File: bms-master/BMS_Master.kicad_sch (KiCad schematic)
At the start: 79 parts, among them J1 Conn_PWR, J2 PROG, J4 BMS_M_IN, J5 Conn_CAN, J6 Conn_CSR, J7 Conn_CSROUT, Q1 BC807, SW1 SW_SPST, U1 AP2204K-ADJ, U2 AP2204K-ADJ, U3 STM32F103C8Tx, U4 BQ79600-Q1, U5 SN65HVD256D, U6 TLV2371DBV, U7 TLV2371DBV, Y1 8M, Y2 32.768k

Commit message: Finish bms_master pcb layout
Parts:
- C30, C31: footprint (none) -> Capacitor_SMD:C_0603_1608Metric
- J7: footprint (none) -> Connector_JST:JST_XH_B3B-XH-A_1x03_P2.50mm_Vertical
- R27, R28: footprint (none) -> Resistor_SMD:R_0603_1608Metric
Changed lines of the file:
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@@
       (effects (font (size 1.27 1.27)) (justify left))
     )
-    (property "Footprint" "" (at 147.955 135.255 0)
+    (property "Footprint" "Capacitor_SMD:C_0603_1608Metric" (at 147.955 135.255 0)
       (effects (font (size 1.27 1.27)) hide)
     )
@@
       (effects (font (size 1.27 1.27)) (justify right))
     )
-    (property "Footprint" "" (at 135.255 173.355 0)
+    (property "Footprint" "Resistor_SMD:R_0603_1608Metric" (at 135.255 173.355 0)
       (effects (font (size 1.27 1.27)) hide)
     )
@@
       (effects (font (size 1.27 1.27)) (justify left))
     )
-    (property "Footprint" "" (at 153.035 184.15 0)
+    (property "Footprint" "Connector_JST:JST_XH_B3B-XH-A_1x03_P2.50mm_Vertical" (at 153.035 184.15 0)
       (effects (font (size 1.27 1.27)) hide)
     )
@@
       (effects (font (size 1.27 1.27)) (justify right))
     )
-    (property "Footprint" "" (at 135.255 179.705 0)
+    (property "Footprint" "Resistor_SMD:R_0603_1608Metric" (at 135.255 179.705 0)
       (effects (font (size 1.27 1.27)) hide)
     )
@@
       (effects (font (size 1.27 1.27)) (justify left))
     )
-    (property "Footprint" "" (at 147.955 163.195 0)
+    (property "Footprint" "Capacitor_SMD:C_0603_1608Metric" (at 147.955 163.195 0)
       (effects (font (size 1.27 1.27)) hide)
     )

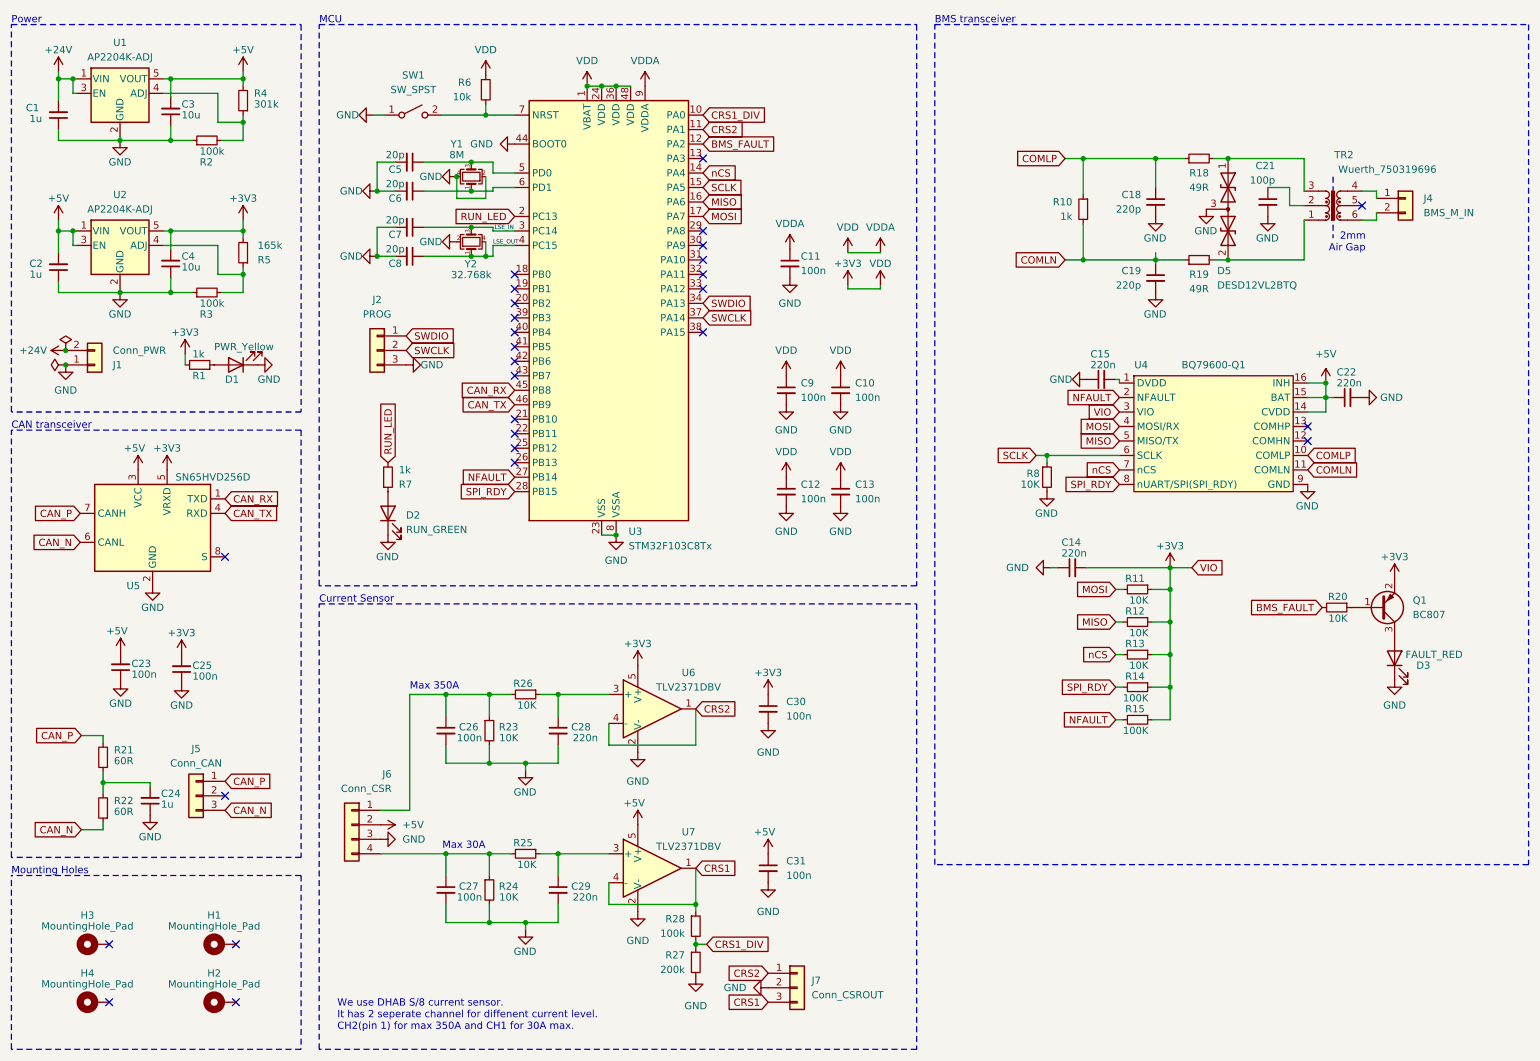
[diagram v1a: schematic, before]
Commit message: Reconfigure file structure and create share lib and 3D CAD
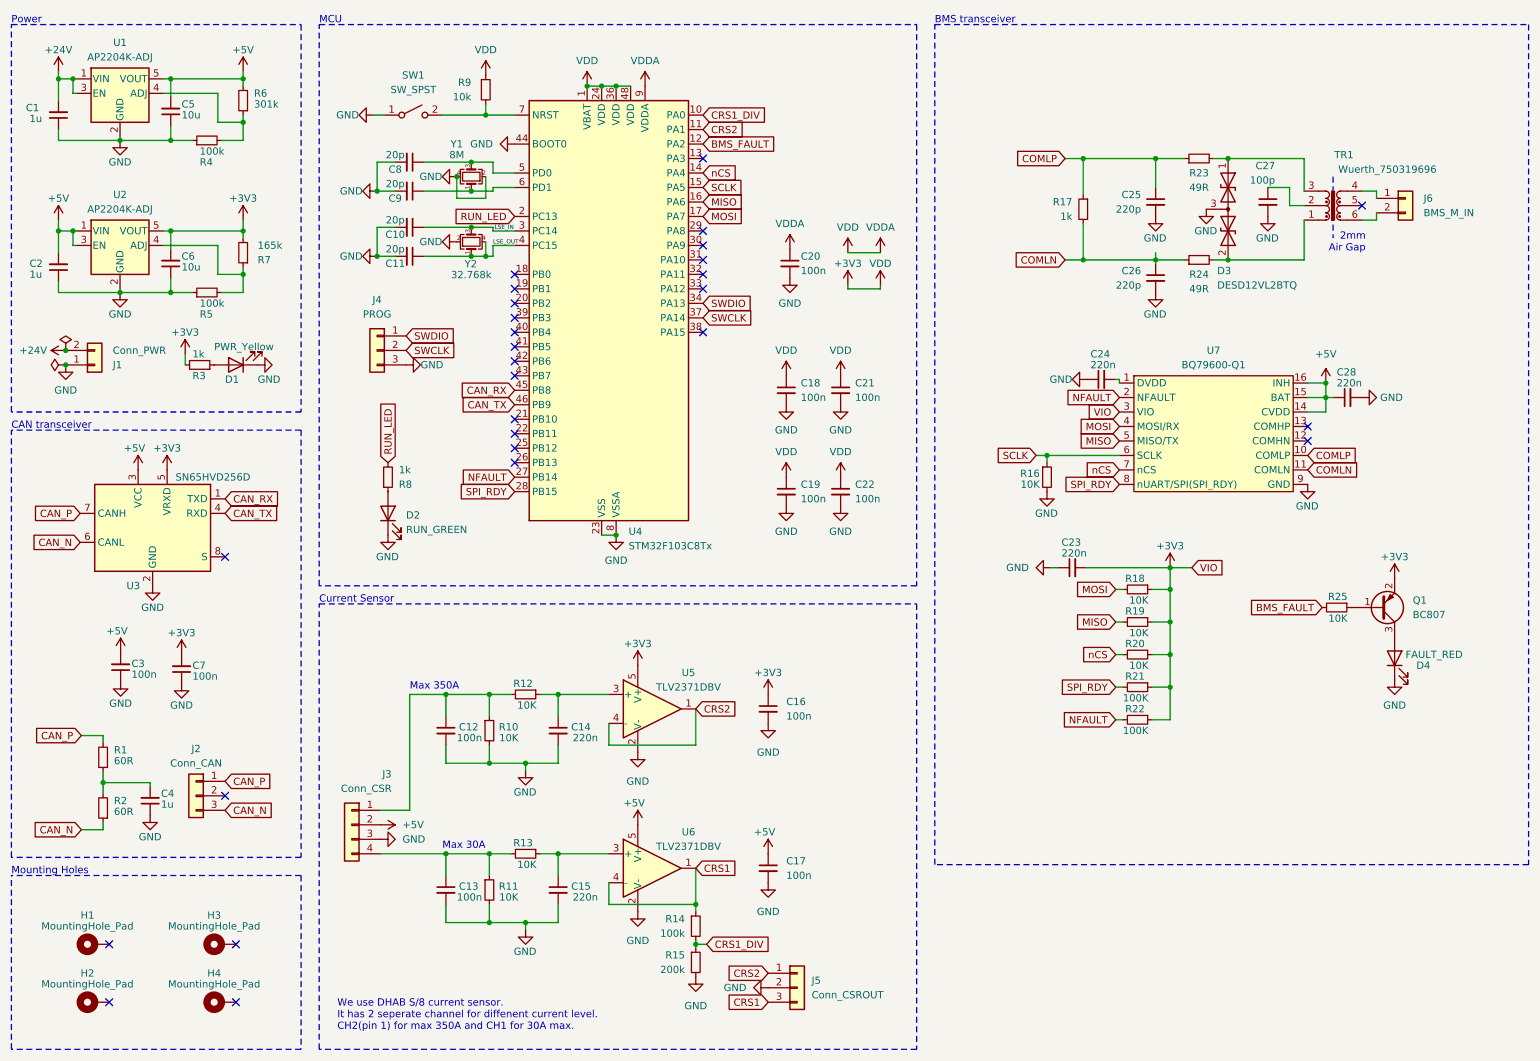
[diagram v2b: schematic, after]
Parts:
- removed U4: BQ79600-Q1, Package_SO:TSSOP-16_4.4x5mm_P0.65mm, symbol Local_Lib:BQ79600-Q1
- added U7: BQ79600-Q1, Package_SO:TSSOP-16_4.4x5mm_P0.65mm, symbol Project_Lib:BQ79600-Q1
- renumbered C7 to C10, C8 to C11, C26 to C12, C27 to C13, C28 to C14, C29 to C15, C30 to C16, C31 to C17, C9 to C18, C12 to C19, C11 to C20, C10 to C21, C13 to C22, C14 to C23, C15 to C24, C18 to C25, C19 to C26, C21 to C27, C22 to C28, C23 to C3, C24 to C4, C3 to C5, C4 to C6, C25 to C7, C5 to C8, C6 to C9, D5 to D3, D3 to D4, H3 to H1, H4 to H2, H1 to H3, H2 to H4, J5 to J2, J6 to J3, J2 to J4, J7 to J5, J4 to J6, R21 to R1, R23 to R10, R24 to R11, R26 to R12, R25 to R13, R28 to R14, R27 to R15, R8 to R16, R10 to R17, R11 to R18, R12 to R19, R22 to R2, R13 to R20, R14 to R21, R15 to R22, R18 to R23, R19 to R24, R20 to R25, R1 to R3, R2 to R4, R3 to R5, R4 to R6, R5 to R7, R7 to R8, R6 to R9, TR2 to TR1, U5 to U3, U3 to U4, U6 to U5, U7 to U6
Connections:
- net +3V3: now also U7.3 (VIO)
- net +5V: now also U7.14 (CVDD), U7.15 (BAT), U7.16 (INH)
- net COMLN: now also U7.11 (COMLN)
- net COMLP: now also U7.10 (COMLP)
- net GND: now also U7.9 (GND)
- net MISO: now also U7.5 (MISO/TX)
- net MOSI: now also U7.4 (MOSI/RX)
- net NFAULT: now also U7.2 (NFAULT)
- net SCLK: now also U7.6 (SCLK)
- net SPI_RDY: now also U7.8 (nUART/SPI(SPI_RDY))
- net nCS: now also U7.7 (nCS)
- net at C24.2: now also U7.1 (DVDD)

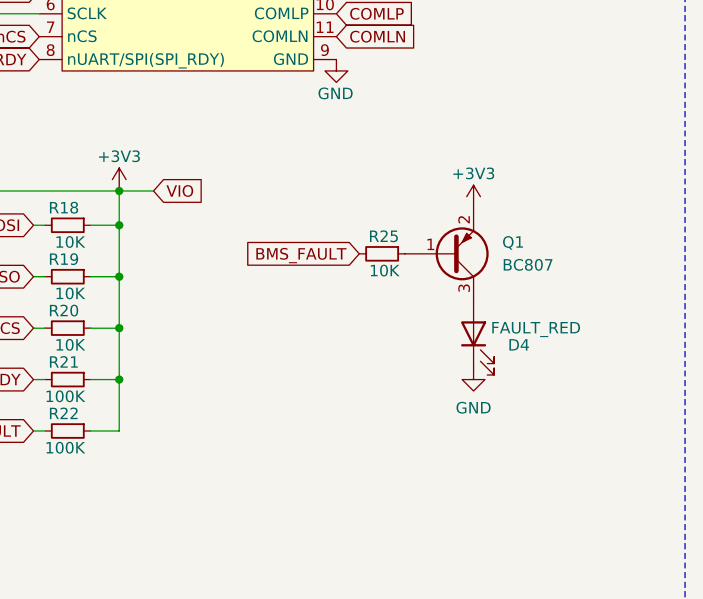
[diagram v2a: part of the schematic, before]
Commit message: fix: add bms fault connector
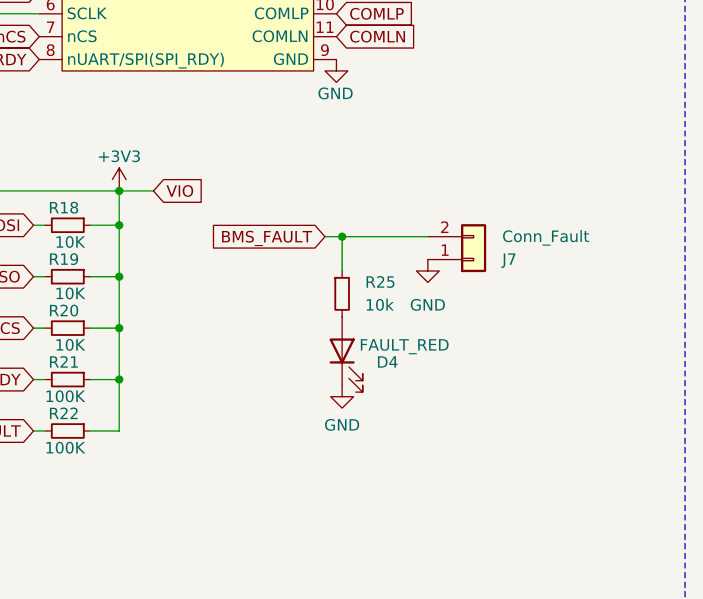
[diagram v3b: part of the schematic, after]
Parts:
- removed Q1: BC807, Package_TO_SOT_SMD:SOT-23, symbol Transistor_BJT:BC807
- added J7: Conn_Fault, Connector_JST:JST_XH_B2B-XH-A_1x02_P2.50mm_Vertical, symbol Connector_Generic:Conn_01x02
- R25: value 10K -> 10k
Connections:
- net BMS_FAULT: now also R25.1, J7.2 (Pin_2); no longer R25.2
- net GND: now also J7.1 (Pin_1)
- net at D4.2 (A): now also R25.2
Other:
- moved on the sheet: D4
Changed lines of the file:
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@@
   (junction (at 93.345 41.91) (diameter 0) (color 0 0 0 0)
   )
+  (junction (at 243.205 115.57) (diameter 0) (color 0 0 0 0)
+  )
   (junction (at 121.285 104.775) (diameter 0) (color 0 0 0 0)
   )
@@
     (stroke (width 0) (type default))
   )
+  (wire (pts (xy 243.205 115.57) (xy 252.73 115.57))
+    (stroke (width 0) (type default))
+  )
   (wire (pts (xy 43.18 51.435) (xy 43.18 54.61))
     (stroke (width 0) (type default))
@@
     (stroke (width 0) (type default))
   )
+  (wire (pts (xy 241.3 115.57) (xy 243.205 115.57))
+    (stroke (width 0) (type default))
+  )
   (wire (pts (xy 239.395 43.815) (xy 235.585 43.815))
     (stroke (width 0) (type default))
@@
     (stroke (width 0) (type default))
   )
+  (wire (pts (xy 243.205 115.57) (xy 243.205 119.38))
+    (stroke (width 0) (type default))
+  )
   (wire (pts (xy 31.3182 155.1686) (xy 31.3182 156.4386))
     (stroke (width 0) (type default))
@@
     (effects (font (size 0.735 0.735)) (justify left bottom))
   )
-  (global_label "BMS_FAULT" (shape input) (at 245.11 117.475 180) (fields_autoplaced)
+  (global_label "BMS_FAULT" (shape input) (at 241.3 115.57 180) (fields_autoplaced)
     (effects (font (size 1.27 1.27)) (justify right))
-    (property "Intersheetrefs" "${INTERSHEET_REFS}" (at 231.7229 117.475 0)
+    (property "Intersheetrefs" "${INTERSHEET_REFS}" (at 227.9129 115.57 0)
       (effects (font (size 1.27 1.27)) (justify right) hide)
     )
@@
     )
   )
-  (symbol (lib_id "power:GND") (at 257.81 130.175 0) (unit 1)
+  (symbol (lib_id "power:GND") (at 243.205 132.08 0) (unit 1)
     (in_bom yes) (on_board yes) (dnp no) (fields_autoplaced)
-    (property "Reference" "#PWR071" (at 257.81 136.525 0)
+    (property "Reference" "#PWR071" (at 243.205 138.43 0)
       (effects (font (size 1.27 1.27)) hide)
     )
-    (property "Value" "GND" (at 257.81 134.62 0)
+    (property "Value" "GND" (at 243.205 136.525 0)
       (effects (font (size 1.27 1.27)))
     )
-    (property "Footprint" "" (at 257.81 130.175 0)
+    (property "Footprint" "" (at 243.205 132.08 0)
       (effects (font (size 1.27 1.27)) hide)
     )
-    (property "Datasheet" "" (at 257.81 130.175 0)
+    (property "Datasheet" "" (at 243.205 132.08 0)
       (effects (font (size 1.27 1.27)) hide)
     )
@@
     )
   )
+  (symbol (lib_id "power:GND") (at 252.73 118.11 0) (unit 1)
+    (in_bom yes) (on_board yes) (dnp no) (fields_autoplaced)
+    (property "Reference" "#PWR070" (at 252.73 124.46 0)
+      (effects (font (size 1.27 1.27)) hide)
+    )
+    (property "Value" "GND" (at 252.73 123.19 0)
+      (effects (font (size 1.27 1.27)))
+    )
+    (property "Footprint" "" (at 252.73 118.11 0)
+      (effects (font (size 1.27 1.27)) hide)
+    )
+    (property "Datasheet" "" (at 252.73 118.11 0)
+      (effects (font (size 1.27 1.27)) hide)
+    )
+    (pin "1")
+    (instances
+      (project "BMS_Master"
+        (path "/a5fe69d4-6cf1-475c-8d8a-0453004bba44"
+          (reference "#PWR070") (unit 1)
+        )
+      )
+    )
+  )
   (symbol (lib_id "power:+5V") (at 55.88 23.495 0) (unit 1)
     (in_bom yes) (on_board yes) (dnp no)
@@
     )
   )
-  (symbol (lib_id "Device:C_Small") (at 45.085 128.27 180) (unit 1)
-    (in_bom yes) (on_board yes) (dnp no)
-    (property "Reference" "C7" (at 46.99 127.635 0)
-      (effects (font (size 1.27 1.27)) (justify right))
+  (symbol (lib_id "Device:R_Small") (at 243.205 121.92 0) (unit 1)
+    (in_bom yes) (on_board yes) (dnp no) (fields_autoplaced)
+    (property "Reference" "R25" (at 245.745 120.65 0)
+      (effects (font (size 1.27 1.27)) (justify left))
     )
-    (property "Value" "100n" (at 46.99 129.54 0)
-      (effects (font (size 1.27 1.27)) (justify right))
+    (property "Value" "10k" (at 245.745 123.19 0)
+      (effects (font (size 1.27 1.27)) (justify left))
     )
-    (property "Footprint" "Capacitor_SMD:C_0603_1608Metric" (at 45.085 128.27 0)
+    (property "Footprint" "Resistor_SMD:R_0603_1608Metric" (at 243.205 121.92 0)
       (effects (font (size 1.27 1.27)) hide)
     )
-    (property "Datasheet" "~" (at 45.085 128.27 0)
+    (property "Datasheet" "~" (at 243.205 121.92 0)
       (effects (font (size 1.27 1.27)) hide)
     )
-    (pin "2")
     (pin "1")
+    (pin "2")
     (instances
       (project "BMS_Master"
         (path "/a5fe69d4-6cf1-475c-8d8a-0453004bba44"
-          (reference "C7") (unit 1)
+          (reference "R25") (unit 1)
         )
       )
     )
   )
-  (symbol (lib_id "Device:R_Small") (at 247.65 117.475 270) (unit 1)
+  (symbol (lib_id "Device:C_Small") (at 45.085 128.27 180) (unit 1)
     (in_bom yes) (on_board yes) (dnp no)
-    (property "Reference" "R25" (at 249.555 115.57 90)
+    (property "Reference" "C7" (at 46.99 127.635 0)
       (effects (font (size 1.27 1.27)) (justify right))
     )
-    (property "Value" "10K" (at 249.555 119.38 90)
+    (property "Value" "100n" (at 46.99 129.54 0)
       (effects (font (size 1.27 1.27)) (justify right))
     )
-    (property "Footprint" "Resistor_SMD:R_0603_1608Metric" (at 247.65 117.475 0)
+    (property "Footprint" "Capacitor_SMD:C_0603_1608Metric" (at 45.085 128.27 0)
       (effects (font (size 1.27 1.27)) hide)
     )
-    (property "Datasheet" "~" (at 247.65 117.475 0)
+    (property "Datasheet" "~" (at 45.085 128.27 0)
       (effects (font (size 1.27 1.27)) hide)
     )
@@
       (project "BMS_Master"
         (path "/a5fe69d4-6cf1-475c-8d8a-0453004bba44"
-          (reference "R25") (unit 1)
+          (reference "C7") (unit 1)
         )
       )
@@
     )
   )
-  (symbol (lib_id "power:+3V3") (at 257.81 112.395 0) (unit 1)
-    (in_bom yes) (on_board yes) (dnp no)
-    (property "Reference" "#PWR070" (at 257.81 116.205 0)
-      (effects (font (size 1.27 1.27)) hide)
-    )
-    (property "Value" "+3V3" (at 257.81 108.585 0)
-      (effects (font (size 1.27 1.27)))
-    )
-    (property "Footprint" "" (at 257.81 112.395 0)
-      (effects (font (size 1.27 1.27)) hide)
-    )
-    (property "Datasheet" "" (at 257.81 112.395 0)
-      (effects (font (size 1.27 1.27)) hide)
-    )
-    (pin "1")
-    (instances
-      (project "BMS_Master"
-        (path "/a5fe69d4-6cf1-475c-8d8a-0453004bba44"
-          (reference "#PWR070") (unit 1)
-        )
-      )
-    )
-  )
   (symbol (lib_id "power:GND") (at 197.485 110.49 270) (unit 1)
     (in_bom yes) (on_board yes) (dnp no)
@@
     )
   )
-  (symbol (lib_id "Device:LED") (at 257.81 126.365 90) (unit 1)
+  (symbol (lib_id "Device:LED") (at 243.205 128.27 90) (unit 1)
     (in_bom yes) (on_board yes) (dnp no)
-    (property "Reference" "D4" (at 261.62 127.635 90)
+    (property "Reference" "D4" (at 247.015 129.54 90)
       (effects (font (size 1.27 1.27)) (justify right))
     )
-    (property "Value" "FAULT_RED" (at 259.715 125.73 90)
+    (property "Value" "FAULT_RED" (at 245.11 127.635 90)
       (effects (font (size 1.27 1.27)) (justify right))
     )
-    (property "Footprint" "LED_SMD:LED_0805_2012Metric" (at 257.81 126.365 0)
+    (property "Footprint" "LED_SMD:LED_0805_2012Metric" (at 243.205 128.27 0)
       (effects (font (size 1.27 1.27)) hide)
     )
-    (property "Datasheet" "~" (at 257.81 126.365 0)
+    (property "Datasheet" "~" (at 243.205 128.27 0)
       (effects (font (size 1.27 1.27)) hide)
     )
@@
     )
   )
+  (symbol (lib_id "Connector_Generic:Conn_01x02") (at 257.81 118.11 0) (mirror x) (unit 1)
+    (in_bom yes) (on_board yes) (dnp no)
+    (property "Reference" "J7" (at 260.985 118.11 0)
+      (effects (font (size 1.27 1.27)) (justify left))
+    )
+    (property "Value" "Conn_Fault" (at 260.985 115.57 0)
+      (effects (font (size 1.27 1.27)) (justify left))
+    )
+    (property "Footprint" "Connector_JST:JST_XH_B2B-XH-A_1x02_P2.50mm_Vertical" (at 257.81 118.11 0)
+      (effects (font (size 1.27 1.27)) hide)
+    )
+    (property "Datasheet" "~" (at 257.81 118.11 0)
+      (effects (font (size 1.27 1.27)) hide)
+    )
+    (pin "1")
+    (pin "2")
+    (instances
+      (project "BMS_Master"
+        (path "/a5fe69d4-6cf1-475c-8d8a-0453004bba44"
+          (reference "J7") (unit 1)
+        )
+      )
+    )
+  )
   (symbol (lib_id "power:VDD") (at 167.64 60.96 0) (unit 1)
     (in_bom yes) (on_board yes) (dnp no)
@@
         )
       )
-    )
-  )
-  (symbol (lib_id "Transistor_BJT:BC807") (at 255.27 117.475 0) (mirror x) (unit 1)
-    (in_bom yes) (on_board yes) (dnp no)
-    (property "Reference" "Q1" (at 260.985 116.205 0)
-      (effects (font (size 1.27 1.27)) (justify left))
-    )
-    (property "Value" "BC807" (at 260.985 118.745 0)
-      (effects (font (size 1.27 1.27)) (justify left))
-    )
-    (property "Footprint" "Package_TO_SOT_SMD:SOT-23" (at 260.35 115.57 0)
-      (effects (font (size 1.27 1.27) italic) (justify left) hide)
-    )
-    (property "Datasheet" "https://www.onsemi.com/pub/Collateral/BC808-D.pdf" (at 255.27 117.475 0)
-      (effects (font (size 1.27 1.27)) (justify left) hide)
-    )
-    (pin "1")
-    (pin "2")
-    (pin "3")
-    (instances
-      (project "BMS_Master"
-        (path "/a5fe69d4-6cf1-475c-8d8a-0453004bba44"
-          (reference "Q1") (unit 1)
-        )
-      )
